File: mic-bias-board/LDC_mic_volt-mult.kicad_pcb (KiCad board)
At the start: 2 copper layers, 38 x 52 mm, 32 parts, among them U1 HCF40106_Hex-Inverter

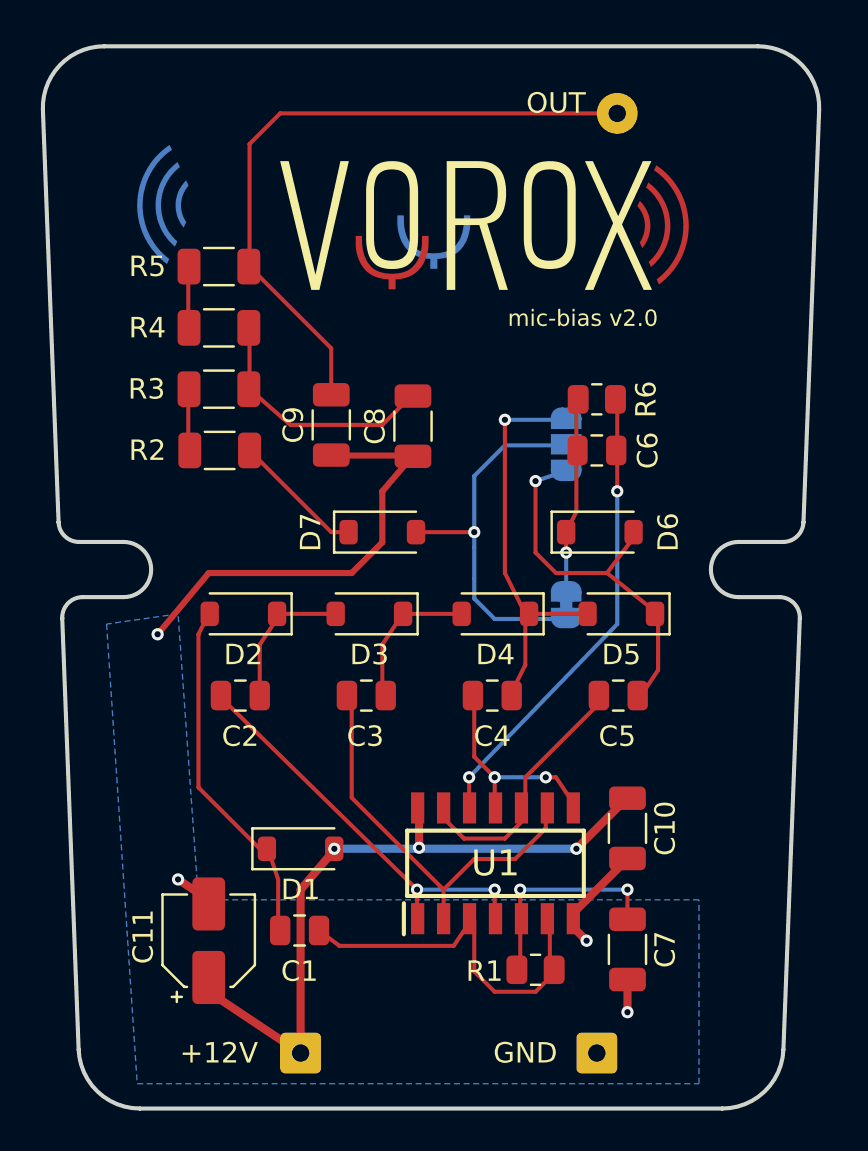
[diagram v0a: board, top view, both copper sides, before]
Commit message: Added panel version of PCB
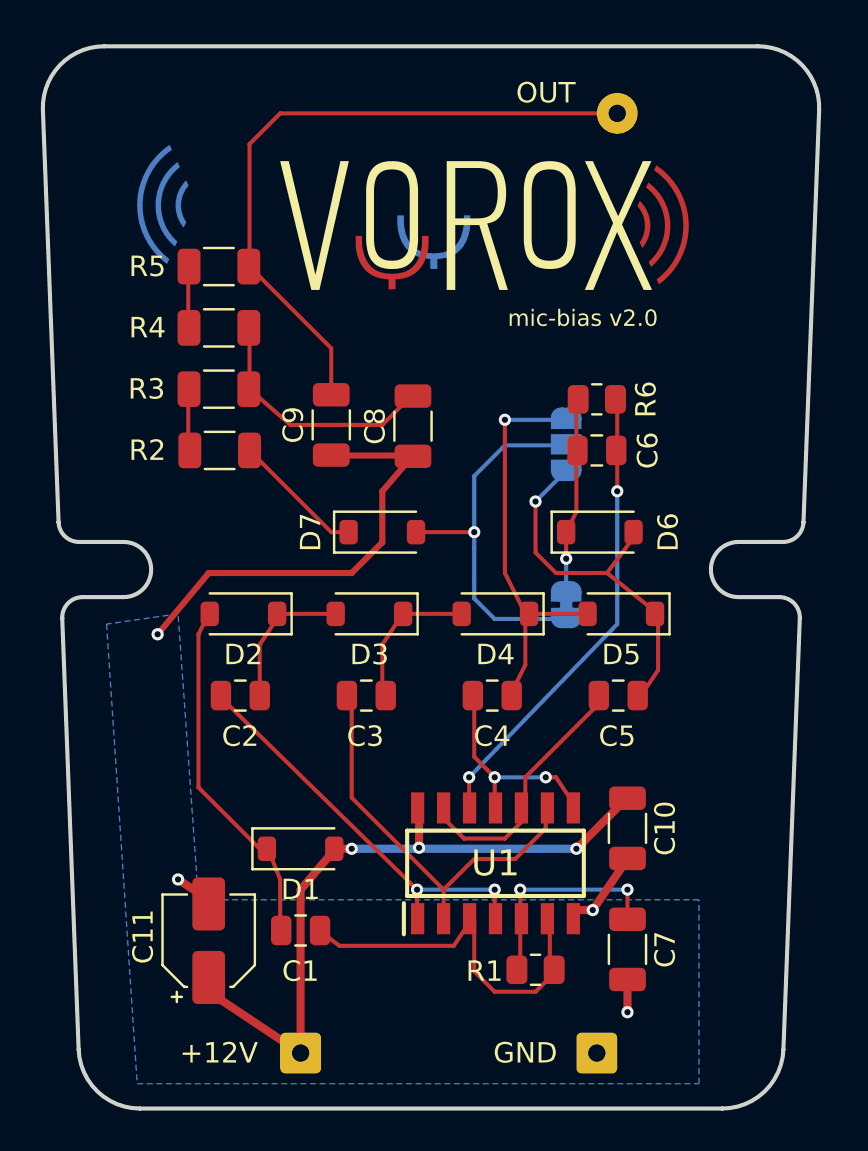
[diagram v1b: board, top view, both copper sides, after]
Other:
- board text added: "Bias voltage selection: 1. CUT the default line (84V) 2. Select new output via the three-way jumper pad (60V or 72V)"
- board text removed: "Bias voltage selection: 1. CUT the default line (84V) 2. Select new output (60V or 72V) via three-way jumper pad"
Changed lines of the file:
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@@
 		(tenting front back)
 		(pcbplotparams
-			(layerselection 0x00000000_00000000_55555555_5755f5ff)
+			(layerselection 0x00000000_00000000_55555555_57555550)
 			(plot_on_all_layers_selection 0x00000000_00000000_00000000_00000000)
 			(disableapertmacros no)
@@
 			(psnegative no)
 			(psa4output no)
-			(plot_black_and_white yes)
+			(plot_black_and_white no)
 			(sketchpadsonfab no)
 			(plotpadnumbers no)
 			(hidednponfab no)
-			(sketchdnponfab yes)
-			(crossoutdnponfab yes)
+			(sketchdnponfab no)
+			(crossoutdnponfab no)
 			(subtractmaskfromsilk no)
-			(outputformat 1)
+			(outputformat 5)
 			(mirror no)
-			(drillshape 1)
+			(drillshape 0)
 			(scaleselection 1)
 			(outputdirectory "")
@@
 	(footprint "Capacitor_SMD:C_0805_2012Metric"
 		(layer "F.Cu")
-		(at 57.45 76)
+		(at 57.5 76)
 		(descr "Capacitor SMD 0805 (2012 Metric), square (rectangular) end terminal, IPC-7351 nominal, (Body size source: IPC-SM-782 page 76, https://www.pcb-3d.com/wordpress/wp-content/uploads/ipc-sm-782a_amendment_1_and_2.pdf, https://docs.google.com/spreadsheets/d/1BsfQQcO9C6DZCsRaXUlFlo91Tg2WpOkGARC1WS5S8t0/edit?usp=sharing), generated with kicad-footprint-generator")
 		(tags "capacitor")
@@
 		(tags "connector wire 0.25sqmm")
 		(property "Reference" "OUT"
-			(at -3 -0.5 0)
+			(at -3.5 -1 0)
 			(layer "F.SilkS")
 			(effects
@@
 	)
 	(gr_line
-		(start 71.5 76.5)
-		(end 71 76)
-		(stroke
-			(width 0.4)
-			(type solid)
-		)
-		(layer "F.Cu")
-		(net 15)
-	)
-	(gr_line
 		(start 67.5 58.5)
 		(end 68.5 60.5)
@@
 	)
 	(gr_line
+		(start 71.8 75)
+		(end 71 75)
+		(stroke
+			(width 0.4)
+			(type solid)
+		)
+		(layer "F.Cu")
+		(net 15)
+	)
+	(gr_line
 		(start 73.5 69.5)
 		(end 71 72)
@@
 	)
 	(gr_line
-		(start 56.4 73.5)
+		(start 56.5 73.5)
 		(end 55.9 72)
 		(stroke
@@
 	)
 	(gr_line
-		(start 71 75)
+		(start 71.8 75)
 		(end 73.5 72.5)
 		(stroke
@@
 	)
 	(gr_line
-		(start 70.5 57.5)
+		(start 70.5 57.8)
 		(end 70.5 56.5)
 		(stroke
 			(width 0.2)
-			(type default)
+			(type solid)
 		)
 		(layer "F.Cu")
@@
 	)
 	(gr_line
+		(start 60 72)
+		(end 59.2 72)
+		(stroke
+			(width 0.4)
+			(type solid)
+		)
+		(layer "F.Cu")
+		(net 1)
+	)
+	(gr_line
 		(start 63.2 74)
 		(end 53.5 64.5)
@@
 	)
 	(gr_line
-		(start 56.4 76.25)
-		(end 56.4 73.5)
+		(start 56.5 76.25)
+		(end 56.5 73.5)
 		(stroke
 			(width 0.2)
@@
 	)
 	(gr_line
-		(start 69 54)
+		(start 69 55)
 		(end 69 57.5)
 		(stroke
@@
 	(gr_line
 		(start 71 72)
-		(end 59.15 72)
+		(end 60 72)
 		(stroke
 			(width 0.4)
@@
 	)
 	(gr_line
-		(start 70.5 57.5)
+		(start 70.5 57.8)
 		(end 70.5 59.5)
 		(stroke
 			(width 0.2)
-			(type default)
+			(type solid)
 		)
 		(layer "B.Cu")
@@
 	)
 	(gr_line
-		(start 69 54)
+		(start 69 55)
 		(end 70.5 53.5)
 		(stroke
@@
 		)
 	)
-	(gr_text "Bias voltage selection:\n1. CUT the default line (84V)\n2. Select new output (60V or 72V)\n   via three-way jumper pad"
-		(at 61 49 90)
+	(gr_text "Bias voltage selection:\n1. CUT the default line (84V)\n2. Select new output via the\n   three-way jumper pad (60V or 72V)"
+		(at 58 49 90)
 		(layer "B.SilkS")
 		(effects
@@
 	)
 	(via
-		(at 59.15 72)
+		(at 60 72)
 		(size 0.6)
 		(drill 0.3)
@@
 	)
 	(via
-		(at 69 54)
+		(at 69 55)
 		(size 0.6)
 		(drill 0.3)
@@
 	)
 	(via
-		(at 70.5 57.5)
+		(at 70.5 57.8)
 		(size 0.6)
 		(drill 0.3)
@@
 	)
 	(via
-		(at 71.5 76.5)
+		(at 71.8 75)
 		(size 0.6)
 		(drill 0.3)

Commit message: Added kikit panel files for two completed projects
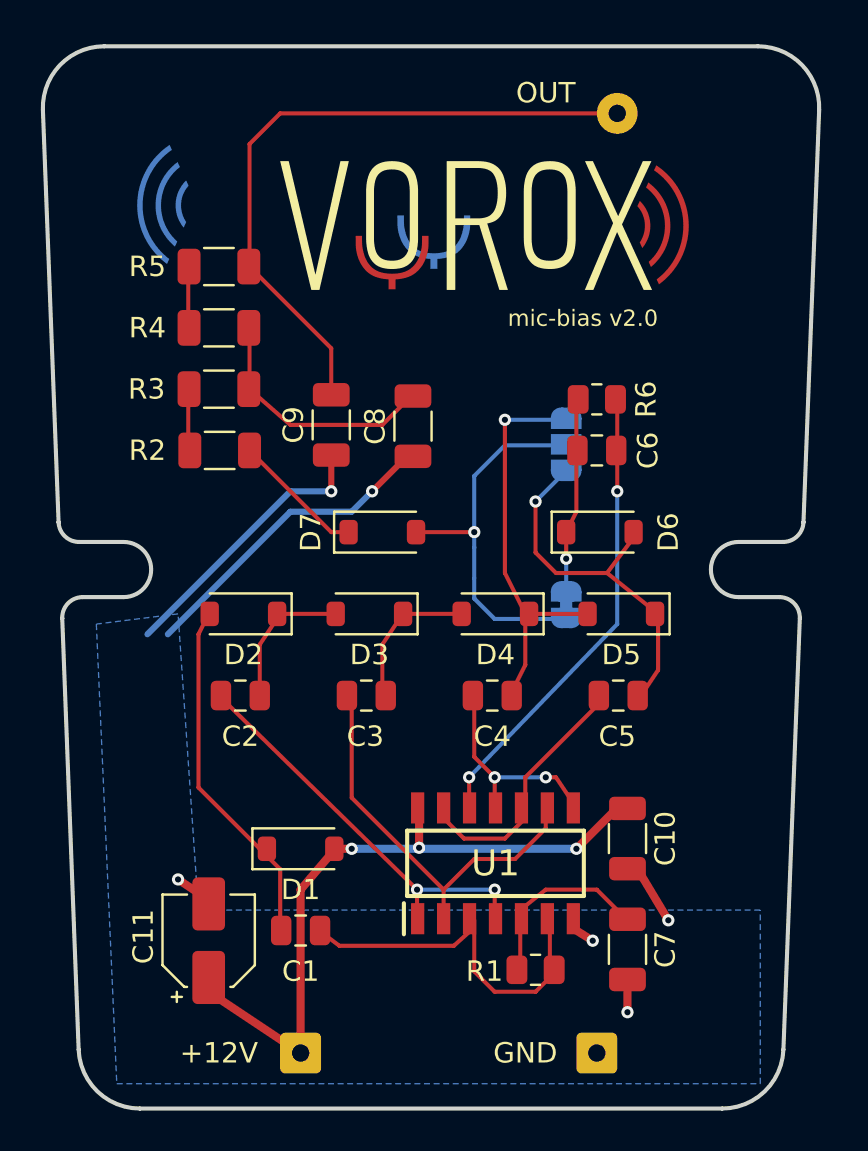
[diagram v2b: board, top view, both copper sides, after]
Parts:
- moved C10 0.50 mm to (73.5, 71.5)
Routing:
- net Net-(U1C-C): vias 2 -> 0
- net GND: vias 4 -> 6
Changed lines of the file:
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@@
 	(footprint "Capacitor_SMD:C_1206_3216Metric"
 		(layer "F.Cu")
-		(at 73.5 71 -90)
+		(at 73.5 71.5 -90)
 		(descr "Capacitor SMD 1206 (3216 Metric), square (rectangular) end terminal, IPC-7351 nominal, (Body size source: IPC-SM-782 page 76, https://www.pcb-3d.com/wordpress/wp-content/uploads/ipc-sm-782a_amendment_1_and_2.pdf), generated with kicad-footprint-generator")
 		(tags "capacitor")
@@
 	)
 	(gr_line
+		(start 59 54.5)
+		(end 59 53)
+		(stroke
+			(width 0.3)
+			(type solid)
+		)
+		(layer "F.Cu")
+		(net 15)
+	)
+	(gr_line
 		(start 67.5 58.5)
 		(end 68.5 60.5)
@@
 	)
 	(gr_line
-		(start 60 58.5)
-		(end 53 58.5)
-		(stroke
-			(width 0.3)
-			(type solid)
-		)
-		(layer "F.Cu")
-		(net 15)
-	)
-	(gr_line
 		(start 55 49.5)
 		(end 55 46.5)
@@
 	)
 	(gr_line
+		(start 62.5 53)
+		(end 61 54.5)
+		(stroke
+			(width 0.3)
+			(type solid)
+		)
+		(layer "F.Cu")
+		(net 15)
+	)
+	(gr_line
 		(start 66 67.5)
 		(end 67 68.5)
@@
 	)
 	(gr_line
-		(start 71.8 75)
-		(end 71 75)
+		(start 71.8 76.5)
+		(end 71 76)
 		(stroke
 			(width 0.4)
@@
 	)
 	(gr_line
-		(start 73.5 69.5)
+		(start 73 70)
 		(end 71 72)
 		(stroke
@@
 	)
 	(gr_line
-		(start 56.5 73.5)
-		(end 55.9 72)
+		(start 56.5 73)
+		(end 55.5 72)
 		(stroke
 			(width 0.2)
@@
 	)
 	(gr_line
-		(start 73.5 74)
-		(end 73.5 75.5)
-		(stroke
-			(width 0.2)
-			(type default)
-		)
-		(layer "F.Cu")
-		(net 6)
-	)
-	(gr_line
-		(start 71.8 75)
-		(end 73.5 72.5)
+		(start 75.5 75.5)
+		(end 74 73)
 		(stroke
 			(width 0.4)
@@
 	)
 	(gr_line
-		(start 68.25 74)
+		(start 69.5 74)
 		(end 68.25 75)
 		(stroke
@@
 	)
 	(gr_line
-		(start 63 52.75)
-		(end 59 52.75)
-		(stroke
-			(width 0.3)
-			(type solid)
-		)
-		(layer "F.Cu")
-		(net 15)
-	)
-	(gr_line
 		(start 70.5 57.8)
 		(end 70.5 56.5)
@@
 	)
 	(gr_line
+		(start 72 74)
+		(end 73 75)
+		(stroke
+			(width 0.2)
+			(type default)
+		)
+		(layer "F.Cu")
+		(net 6)
+	)
+	(gr_line
 		(start 52.5 69)
 		(end 55.5 72)
@@
 	)
 	(gr_line
-		(start 63 52.75)
-		(end 61.5 54.5)
-		(stroke
-			(width 0.3)
-			(type solid)
-		)
-		(layer "F.Cu")
-		(net 15)
-	)
-	(gr_line
 		(start 71 55.5)
 		(end 70.5 56.5)
@@
 	(gr_line
 		(start 65 76.75)
-		(end 65.833333 75.5)
+		(end 65.833333 76)
 		(stroke
 			(width 0.2)
@@
 	)
 	(gr_line
+		(start 69.5 74)
+		(end 72 74)
+		(stroke
+			(width 0.2)
+			(type default)
+		)
+		(layer "F.Cu")
+		(net 6)
+	)
+	(gr_line
 		(start 71 50)
 		(end 71 52.5)
@@
 	)
 	(gr_line
-		(start 61.5 54.5)
-		(end 61.5 57)
-		(stroke
-			(width 0.3)
-			(type solid)
-		)
-		(layer "F.Cu")
-		(net 15)
-	)
-	(gr_line
-		(start 61.5 57)
-		(end 60 58.5)
-		(stroke
-			(width 0.3)
-			(type solid)
-		)
-		(layer "F.Cu")
-		(net 15)
-	)
-	(gr_line
 		(start 64.5 74)
 		(end 60 69.5)
@@
 	(gr_line
 		(start 56.5 76.25)
-		(end 56.5 73.5)
+		(end 56.5 73)
 		(stroke
 			(width 0.2)
@@
 	)
 	(gr_line
-		(start 53 58.5)
-		(end 50.5 61.5)
+		(start 60 55.5)
+		(end 57 55.5)
 		(stroke
 			(width 0.3)
 			(type solid)
 		)
-		(layer "F.Cu")
+		(layer "B.Cu")
 		(net 15)
 	)
@@
 	)
 	(gr_line
+		(start 50 61.5)
+		(end 57 54.5)
+		(stroke
+			(width 0.3)
+			(type solid)
+		)
+		(layer "B.Cu")
+		(net 15)
+	)
+	(gr_line
 		(start 66 58.75)
 		(end 66 59.75)
@@
 	)
 	(gr_line
-		(start 73.5 74)
-		(end 68.5 74)
-		(stroke
-			(width 0.2)
-			(type default)
-		)
-		(layer "B.Cu")
-		(net 6)
-	)
-	(gr_line
 		(start 69 55)
 		(end 70.5 53.5)
@@
 	)
 	(gr_line
+		(start 61 54.5)
+		(end 60 55.5)
+		(stroke
+			(width 0.3)
+			(type solid)
+		)
+		(layer "B.Cu")
+		(net 15)
+	)
+	(gr_line
+		(start 57 54.5)
+		(end 59 54.5)
+		(stroke
+			(width 0.3)
+			(type solid)
+		)
+		(layer "B.Cu")
+		(net 15)
+	)
+	(gr_line
+		(start 57 55.5)
+		(end 51 61.5)
+		(stroke
+			(width 0.3)
+			(type solid)
+		)
+		(layer "B.Cu")
+		(net 15)
+	)
+	(gr_line
 		(start 67.5 52.25)
 		(end 66 53.75)
@@
 	)
 	(via
-		(at 68.25 74)
-		(size 0.6)
-		(drill 0.3)
-		(layers "F.Cu" "B.Cu")
-		(net 6)
-	)
-	(via
-		(at 73.5 74)
-		(size 0.6)
-		(drill 0.3)
-		(layers "F.Cu" "B.Cu")
-		(net 6)
-	)
-	(via
 		(at 67.5 51)
 		(size 0.6)
@@
 	)
 	(via
-		(at 71.8 75)
+		(at 59 54.5)
 		(size 0.6)
 		(drill 0.3)
 		(layers "F.Cu" "B.Cu")
-		(free yes)
 		(net 15)
 	)
 	(via
-		(at 50.5 61.5)
+		(at 75.5 75.5)
 		(size 0.6)
 		(drill 0.3)
 		(layers "F.Cu" "B.Cu")
+		(free yes)
 		(net 15)
 	)
@@
 	)
 	(via
+		(at 61 54.5)
+		(size 0.6)
+		(drill 0.3)
+		(layers "F.Cu" "B.Cu")
+		(net 15)
+	)
+	(via
 		(at 73.5 80)
 		(size 0.6)
@@
 	)
 	(via
+		(at 71.8 76.5)
+		(size 0.6)
+		(drill 0.3)
+		(layers "F.Cu" "B.Cu")
+		(net 15)
+	)
+	(via
 		(at 66 56.5)
 		(size 0.6)
@@
 		(polygon
 			(pts
-				(xy 52.5 74.5) (xy 51.5 60.5) (xy 48 61) (xy 49.5 83.5) (xy 77 83.5) (xy 77 74.5)
+				(xy 52.5 75) (xy 51.5 60.5) (xy 47.5 61) (xy 48.5 83.5) (xy 80 83.5) (xy 80 75)
 			)
 		)
